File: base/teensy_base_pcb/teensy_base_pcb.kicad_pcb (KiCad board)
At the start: 2 copper layers, 69.8 x 48.3 mm, 28 parts, among them Q1 PN2222A, U1 LM7805CT, U2 LD1117V33, U3 Teensy_3.2, U4 nRF24L01+

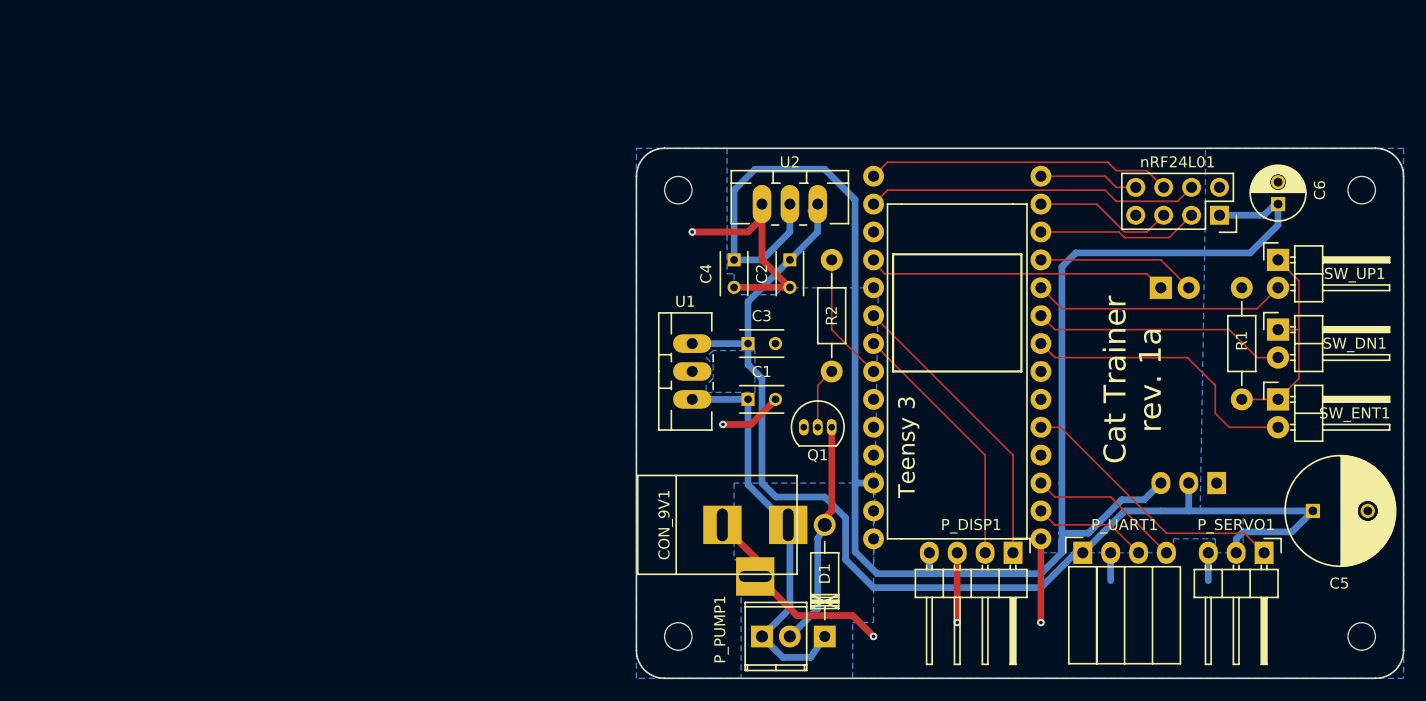
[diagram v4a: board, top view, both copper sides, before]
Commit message: Update PCB layout for TA8428K motor driver.
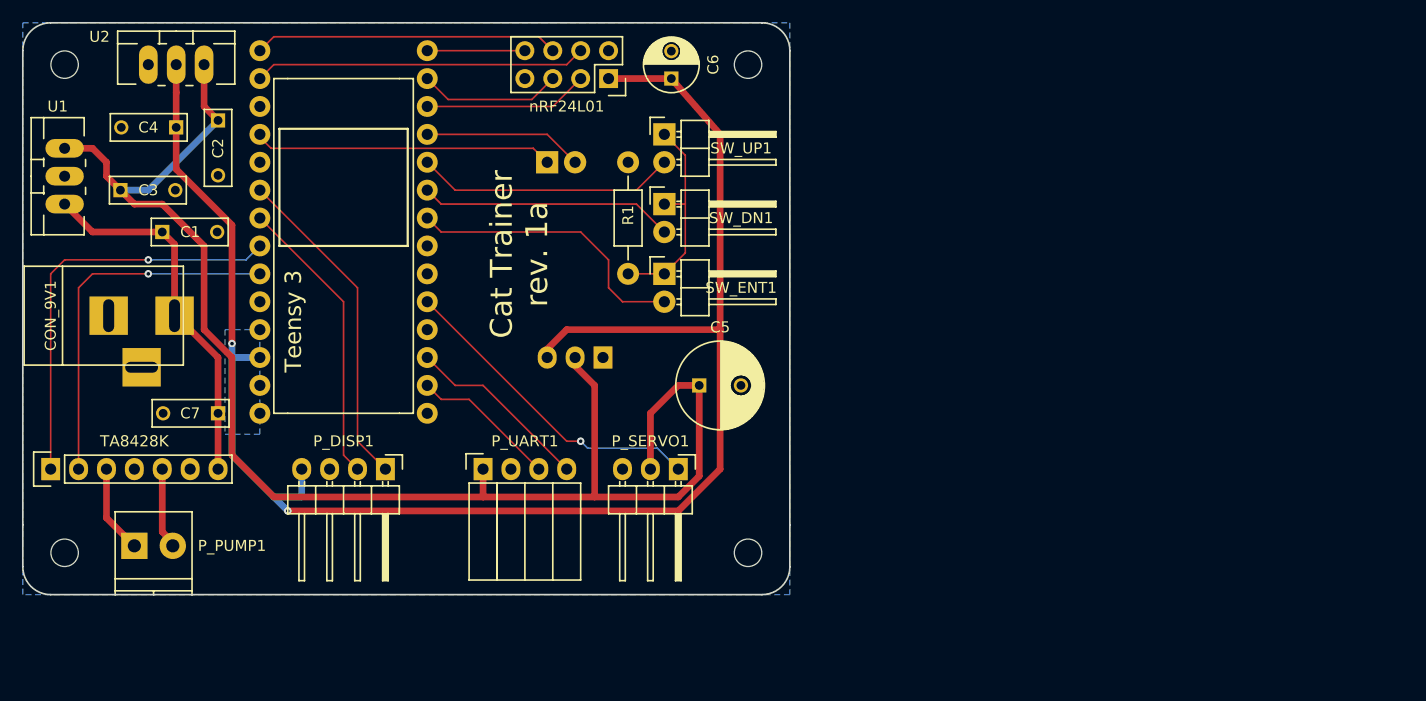
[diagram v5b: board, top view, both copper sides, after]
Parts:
- removed D1: 1N4004, Diodes_ThroughHole:Diode_DO-41_SOD81_Horizontal_RM10
- removed Q1: PN2222A, TO_SOT_Packages_THT:TO-92_Inline_Narrow_Oval
- removed R2: 270, Resistors_ThroughHole:Resistor_Horizontal_RM10mm
- added C7: 10uF, Capacitors_ThroughHole:C_Rect_L7_W2.5_P5, F.Cu at (120.7, 105.4)
- added U5: TA8428K, Socket_Strips:Socket_Strip_Straight_1x07, F.Cu at (105.4, 110.5)
- C1, C2, C3, C4: footprint Capacitors_ThroughHole:C_Rect_L4_W2.5_P2.5 -> Capacitors_ThroughHole:C_Rect_L7_W2.5_P5
- C5: footprint Capacitors_ThroughHole:C_Radial_D10_L20_P5 -> Capacitors_ThroughHole:C_Radial_D8_L13_P3.8
- C6: footprint Capacitors_ThroughHole:C_Radial_D5_L11_P2 -> Capacitors_ThroughHole:C_Radial_D5_L11_P2.5
- P_PUMP1: footprint Terminal_Blocks:TerminalBlock_Pheonix_MPT-2.54mm_2pol -> Terminal_Blocks:TerminalBlock_Pheonix_PT-3.5mm_2pol
- moved U1 59.9 mm to (106.7, 83.8)
- moved CON_9V1 59.0 mm to (110.5, 96.5)
- moved C3 58.8 mm to (111.8, 85.1)
- moved P_PUMP1 57.7 mm to (113.0, 117.5)
- moved P_DISP1 57.7 mm to (135.9, 110.5)
- moved U2 57.3 mm to (116.8, 73.7)
- moved U3 57.0 mm to (139.7, 102.9)
- moved C5 57.0 mm to (164.5, 102.9)
- moved P_ACC1 57.0 mm to (155.7, 100.3)
- moved P_ACC2 57.0 mm to (150.6, 82.5)
- moved R1 57.0 mm to (158.0, 92.7)
- moved REF** 57.0 mm to (168.9, 73.7)
- moved REF** 57.0 mm to (106.7, 73.7)
- moved SW_DN1 57.0 mm to (161.3, 86.4)
- moved SW_ENT1 57.0 mm to (161.3, 92.7)
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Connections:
- P_PUMP1 pad 1: +9V -> Net-(P_PUMP1-Pad1)
- U3 pad 21: NC -> Net-(U3-Pad21)
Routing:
- net GND: track 65.7 -> 0.00 mm, vias 5 -> 0
- net Net-(U3-Pad21): track 0.00 -> 33.5 mm, vias 0 -> 1
- net +5V: track 105.6 -> 135.3 mm
- net Net-(U3-Pad20): track 11.7 -> 37.9 mm, vias 0 -> 1
- net Net-(P_PUMP1-Pad2): track 20.5 -> 7.69 mm
- net Net-(P_PUMP1-Pad1): track 0.00 -> 8.04 mm
- net Net-(Q1-Pad2): track 5.61 -> 0.00 mm
- net Net-(P_SERVO1-Pad1): track 25.1 -> 29.2 mm, vias 0 -> 1
- net +3.3V: track 151.3 -> 155.1 mm, vias 0 -> 2
- net Net-(P_DISP1-Pad2): track 23.3 -> 26.5 mm
- net Net-(P_DISP1-Pad1): track 26.9 -> 30.1 mm
- net +9V: track 36.8 -> 33.7 mm
- net Net-(P_UART1-Pad4): track 14.1 -> 16.9 mm
- net Net-(P_UART1-Pad3): track 10.5 -> 13.3 mm
- net Net-(SW_UP1-Pad2): track 23.2 -> 23.7 mm
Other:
- board size 69.8 x 48.3 mm -> 69.9 x 52.1 mm
- board text added: "TA8428K"

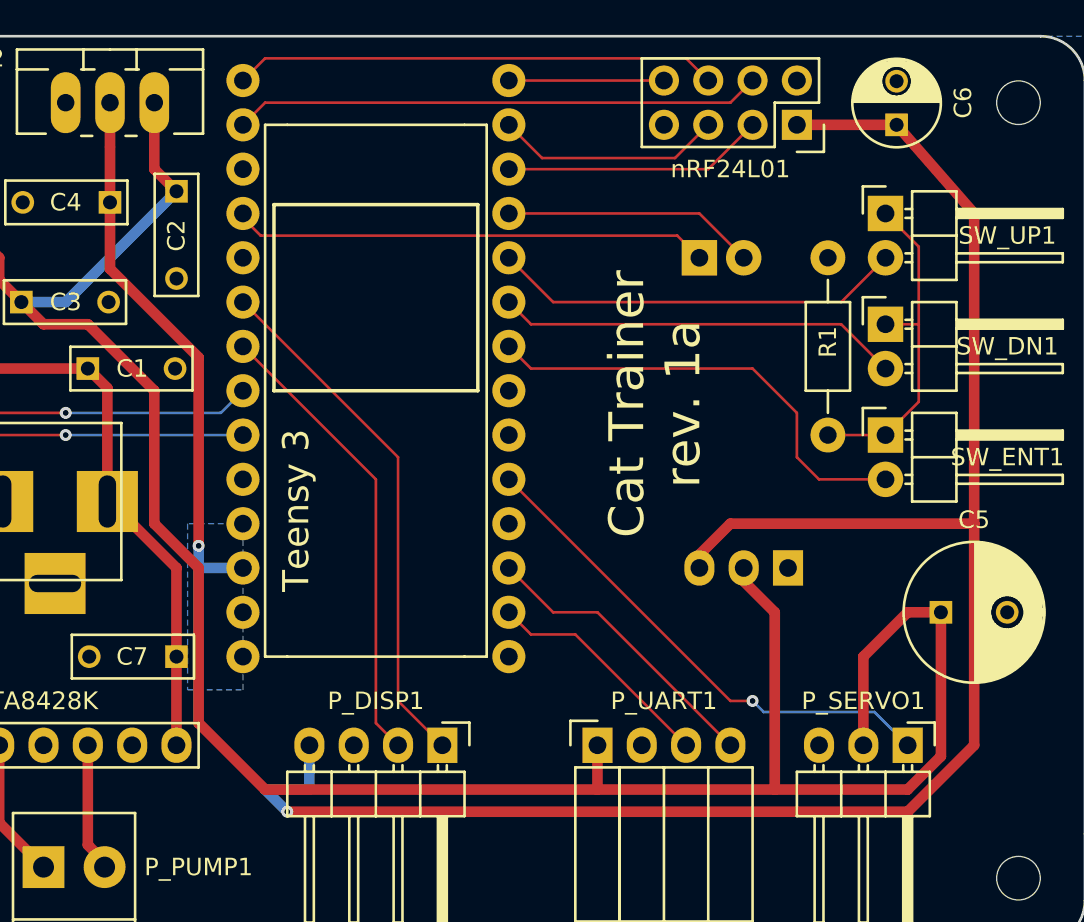
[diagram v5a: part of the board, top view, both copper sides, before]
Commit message: Clean up traces and fill areas.
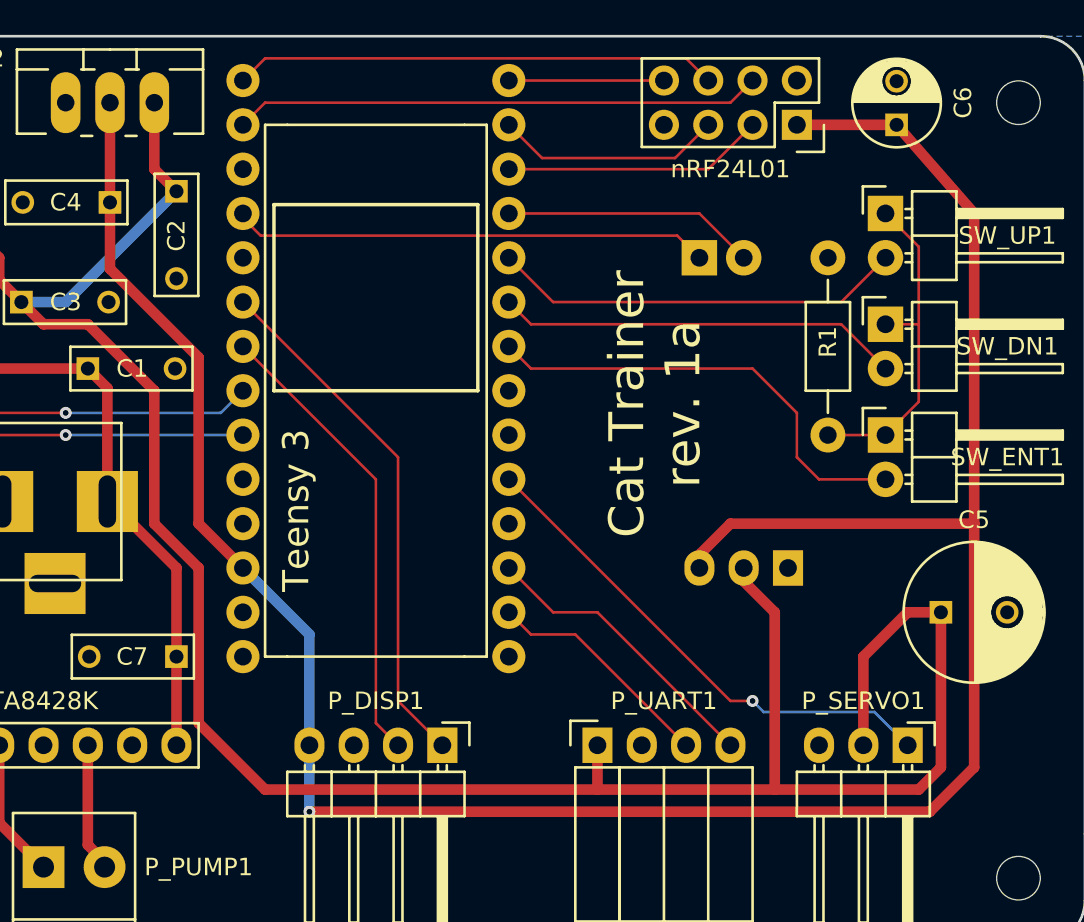
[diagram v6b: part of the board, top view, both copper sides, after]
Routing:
- net +3.3V: track 155.1 -> 147.5 mm, vias 2 -> 1
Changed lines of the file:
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@@
     (links 66)
     (no_connects 9)
-    (area 102.794999 69.774999 172.795001 121.995001)
+    (area 98.599029 69.2326 192.305715 135.415001)
     (thickness 1.6)
     (drawings 28)
-    (tracks 133)
+    (tracks 128)
     (zones 0)
     (modules 27)
@@
   (segment (start 116.84 96.52) (end 120.65 100.33) (width 0.6096) (layer F.Cu) (net 13) (status 10))
   (segment (start 120.65 100.33) (end 120.65 105.41) (width 0.6096) (layer F.Cu) (net 13) (status 20))
-  (segment (start 120.65 105.41) (end 120.65 110.49) (width 0.6096) (layer F.Cu) (net 13) (status 10))
+  (segment (start 120.65 105.41) (end 120.65 110.49) (width 0.6096) (layer F.Cu) (net 13) (status 30))
   (segment (start 116.69014 96.52) (end 116.69014 90.02014) (width 0.6096) (layer F.Cu) (net 13) (status 10))
   (segment (start 116.69014 90.02014) (end 115.57 88.9) (width 0.6096) (layer F.Cu) (net 13) (status 20))
   (segment (start 115.57 88.9) (end 109.22 88.9) (width 0.6096) (layer F.Cu) (net 13) (status 10))
   (segment (start 109.22 88.9) (end 106.68 86.36) (width 0.6096) (layer F.Cu) (net 13) (status 20))
-  (segment (start 111.76 85.09) (end 114.3 85.09) (width 0.6096) (layer B.Cu) (net 14))
-  (segment (start 114.3 85.09) (end 120.65 78.74) (width 0.6096) (layer B.Cu) (net 14))
+  (segment (start 164.465 102.87) (end 164.465 111.76) (width 0.6096) (layer F.Cu) (net 14) (status 10))
+  (segment (start 163.195 113.03) (end 154.94 113.03) (width 0.6096) (layer F.Cu) (net 14))
+  (segment (start 164.465 111.76) (end 163.195 113.03) (width 0.6096) (layer F.Cu) (net 14))
+  (segment (start 111.76 85.09) (end 114.3 85.09) (width 0.6096) (layer B.Cu) (net 14) (status 10))
+  (segment (start 114.3 85.09) (end 120.65 78.74) (width 0.6096) (layer B.Cu) (net 14) (status 20))
   (segment (start 125.73 113.03) (end 144.78 113.03) (width 0.6096) (layer F.Cu) (net 14))
   (segment (start 144.78 113.03) (end 144.78 110.49) (width 0.6096) (layer F.Cu) (net 14) (status 20))
@@
   (segment (start 154.94 102.87) (end 154.94 113.03) (width 0.6096) (layer F.Cu) (net 14))
   (segment (start 144.78 113.03) (end 154.94 113.03) (width 0.6096) (layer F.Cu) (net 14))
-  (segment (start 154.94 113.03) (end 162.56 113.03) (width 0.6096) (layer F.Cu) (net 14))
-  (segment (start 164.465 111.125) (end 164.465 102.87) (width 0.6096) (layer F.Cu) (net 14) (status 20))
-  (segment (start 162.56 113.03) (end 164.465 111.125) (width 0.6096) (layer F.Cu) (net 14))
   (segment (start 113.03 86.36) (end 115.57 86.36) (width 0.6096) (layer F.Cu) (net 14))
   (segment (start 115.57 86.36) (end 119.38 90.17) (width 0.6096) (layer F.Cu) (net 14))
@@
   (segment (start 120.65 78.74) (end 119.38 77.47) (width 0.6096) (layer F.Cu) (net 14) (status 10))
   (segment (start 119.38 77.47) (end 119.38 73.66) (width 0.6096) (layer F.Cu) (net 14) (status 20))
+  (segment (start 128.27 104.14) (end 128.27 110.49) (width 0.6096) (layer B.Cu) (net 15))
+  (segment (start 124.46 100.33) (end 128.27 104.14) (width 0.6096) (layer B.Cu) (net 15))
+  (segment (start 128.27 110.49) (end 128.27 114.3) (width 0.6096) (layer B.Cu) (net 15))
+  (segment (start 128.27 114.3) (end 163.83 114.3) (width 0.6096) (layer F.Cu) (net 15))
+  (segment (start 166.37 111.76) (end 163.83 114.3) (width 0.6096) (layer F.Cu) (net 15))
+  (segment (start 166.37 97.79) (end 166.37 111.76) (width 0.6096) (layer F.Cu) (net 15))
+  (via (at 128.27 114.3) (size 0.6858) (drill 0.3302) (layers F.Cu B.Cu) (net 15))
+  (segment (start 124.46 100.33) (end 121.92 97.79) (width 0.6096) (layer F.Cu) (net 15))
   (segment (start 121.92 88.265) (end 116.84 83.185) (width 0.6096) (layer F.Cu) (net 15))
-  (via (at 121.92 99.06) (size 0.6858) (drill 0.3302) (layers F.Cu B.Cu) (net 15))
-  (segment (start 121.92 100.33) (end 121.92 99.06) (width 0.6096) (layer B.Cu) (net 15))
-  (segment (start 121.92 99.06) (end 121.92 88.265) (width 0.6096) (layer F.Cu) (net 15))
-  (segment (start 116.84 83.185) (end 116.84 79.375) (width 0.6096) (layer F.Cu) (net 15))
+  (segment (start 116.84 83.185) (end 116.84 79.375) (width 0.6096) (layer F.Cu) (net 15) (status 20))
+  (segment (start 121.92 97.79) (end 121.92 88.265) (width 0.6096) (layer F.Cu) (net 15))
   (segment (start 166.37 97.79) (end 152.4 97.79) (width 0.6096) (layer F.Cu) (net 15))
   (segment (start 152.4 97.79) (end 150.622 99.568) (width 0.6096) (layer F.Cu) (net 15) (status 20))
   (segment (start 150.622 99.568) (end 150.622 100.33) (width 0.6096) (layer F.Cu) (net 15) (status 30))
-  (segment (start 125.73 113.03) (end 127 114.3) (width 0.6096) (layer B.Cu) (net 15))
   (segment (start 166.37 80.01) (end 161.925 74.93) (width 0.6096) (layer F.Cu) (net 15) (status 20))
-  (segment (start 166.37 110.49) (end 166.37 97.79) (width 0.6096) (layer F.Cu) (net 15))
   (segment (start 166.37 97.79) (end 166.37 80.01) (width 0.6096) (layer F.Cu) (net 15))
-  (segment (start 162.56 114.3) (end 166.37 110.49) (width 0.6096) (layer F.Cu) (net 15))
-  (segment (start 127 114.3) (end 162.56 114.3) (width 0.6096) (layer F.Cu) (net 15))
-  (via (at 127 114.3) (size 0.6858) (drill 0.3302) (layers F.Cu B.Cu) (net 15))
-  (segment (start 161.925 74.93) (end 156.21 74.93) (width 0.6096) (layer F.Cu) (net 15) (status 10))
+  (segment (start 161.925 74.93) (end 156.21 74.93) (width 0.6096) (layer F.Cu) (net 15) (status 30))
   (segment (start 150.622 100.33) (end 150.622 99.568) (width 0.6096) (layer B.Cu) (net 15) (status 30))
-  (segment (start 121.92 100.33) (end 124.46 100.33) (width 0.6096) (layer B.Cu) (net 15) (status 20))
-  (segment (start 128.27 110.49) (end 128.27 113.03) (width 0.6096) (layer B.Cu) (net 15) (status 10))
-  (segment (start 121.92 100.33) (end 121.92 109.22) (width 0.6096) (layer B.Cu) (net 15))
-  (segment (start 121.92 109.22) (end 125.73 113.03) (width 0.6096) (layer B.Cu) (net 15))
-  (segment (start 125.73 113.03) (end 128.27 113.03) (width 0.6096) (layer B.Cu) (net 15))
-  (segment (start 116.84 73.66) (end 116.84 76.2) (width 0.6096) (layer F.Cu) (net 15) (status 10))
-  (segment (start 116.84 76.2) (end 116.84 79.375) (width 0.6096) (layer F.Cu) (net 15) (status 20))
+  (segment (start 116.84 73.66) (end 116.84 79.375) (width 0.6096) (layer F.Cu) (net 15) (status 30))
   (segment (start 128.27 110.49) (end 128.27 111.125) (width 0.6096) (layer B.Cu) (net 15) (status 30))
   (segment (start 128.27 111.125) (end 128.27 110.998) (width 0.6096) (layer B.Cu) (net 15) (status 30))
@@
   (segment (start 139.7 80.01) (end 150.622 80.01) (width 0.1524) (layer F.Cu) (net 21) (status 10))
   (segment (start 150.622 80.01) (end 153.162 82.55) (width 0.1524) (layer F.Cu) (net 21) (status 20))
-  (segment (start 115.57 110.49) (end 115.57 116.205) (width 0.6096) (layer F.Cu) (net 22))
-  (segment (start 115.57 116.205) (end 116.53 117.165) (width 0.6096) (layer F.Cu) (net 22))
-  (segment (start 116.53 117.165) (end 116.53 117.475) (width 0.6096) (layer F.Cu) (net 22))
+  (segment (start 115.57 110.49) (end 115.57 116.205) (width 0.6096) (layer F.Cu) (net 22) (status 10))
+  (segment (start 115.57 116.205) (end 116.53 117.165) (width 0.6096) (layer F.Cu) (net 22) (status 20))
+  (segment (start 116.53 117.165) (end 116.53 117.475) (width 0.6096) (layer F.Cu) (net 22) (status 30))
   (segment (start 116.53 117.475) (end 116.53 117.165) (width 0.1524) (layer F.Cu) (net 22) (status 30))
-  (segment (start 110.49 110.49) (end 110.49 114.935) (width 0.6096) (layer F.Cu) (net 23))
-  (segment (start 110.49 114.935) (end 113.03 117.475) (width 0.6096) (layer F.Cu) (net 23))
+  (segment (start 110.49 110.49) (end 110.49 114.935) (width 0.6096) (layer F.Cu) (net 23) (status 10))
+  (segment (start 110.49 114.935) (end 113.03 117.475) (width 0.6096) (layer F.Cu) (net 23) (status 20))
   (segment (start 124.46 90.17) (end 123.19 91.44) (width 0.1524) (layer B.Cu) (net 24) (status 10))
   (segment (start 105.41 92.71) (end 105.41 110.49) (width 0.1524) (layer F.Cu) (net 24) (status 20))
@@
       )
     )
-    (polygon
-      (pts        (xy 121.285 97.79) (xy 121.285 107.315) (xy 124.46 107.315) (xy 124.46 97.79)
-      )
-    )

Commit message: Add resettable fuse / clean up traces / widths.
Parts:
- added F1: F_Small, Fuse_Holders_and_Fuses:Fuse_TE5_Littlefuse-395Series, F.Cu at (117.5, 105.4)
- moved C7 10.2 mm to (110.5, 105.4)
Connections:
- C7 pad 1: +9V -> Net-(C7-Pad1)
- U5 pad 7: +9V -> Net-(C7-Pad1)
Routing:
- net Net-(C7-Pad1): track 0.00 -> 16.7 mm
- net +9V: track 33.7 -> 28.4 mm
- net +5V: track 135.7 -> 137.1 mm
- net Net-(U3-Pad20): track 37.9 -> 36.8 mm
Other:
- net class Current added: clearance 0.2032, trace_width 0.9652, via_dia 0.6858, via_drill 0.3302
- net class Power: via_dia 0.6858 -> 0.9398; via_drill 0.3302 -> 0.5842

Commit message: Swap servo output pins and clean up traces.
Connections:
- P_SERVO1 pad 1: Net-(P_SERVO1-Pad1) -> GND
- P_SERVO1 pad 3: GND -> Net-(P_SERVO1-Pad3)
- U3 pad 3: Net-(P_SERVO1-Pad1) -> Net-(P_SERVO1-Pad3)
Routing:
- net Net-(P_SERVO1-Pad1): track 29.2 -> 0.00 mm, vias 1 -> 0
- net Net-(P_SERVO1-Pad3): track 0.00 -> 24.1 mm
- net +5V: track 137.1 -> 133.5 mm
